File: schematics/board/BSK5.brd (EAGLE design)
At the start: 94 x 94 mm, 18 parts

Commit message: Новые схемы
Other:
- board text added: "BSK5 "Концерн ИТС""
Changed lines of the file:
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@@
 <text x="65.6" y="30.1" size="1.4224" layer="26" rot="MR0">BUS-</text>
 <text x="33.2" y="30.2" size="1.4224" layer="26" rot="MR0">BUS-</text>
+<text x="19.9" y="65.1" size="1.4224" layer="25" rot="MR45">BUS+</text>
+<text x="78.3" y="69.2" size="1.4224" layer="26" rot="MR315">BUS+</text>
+<text x="66.3" y="20.6" size="1.4224" layer="26" rot="MR225">BUS+</text>
+<text x="23.7" y="16.5" size="1.4224" layer="26" rot="MR135">BUS+</text>
+<text x="28.7" y="56.5" size="1.4224" layer="26" rot="MR45">BUS-</text>
+<text x="68.2" y="59.3" size="1.4224" layer="26" rot="MR315">BUS-</text>
+<text x="58.3" y="28.7" size="1.4224" layer="26" rot="MR225">BUS-</text>
+<text x="32.2" y="25" size="1.4224" layer="26" rot="MR135">BUS-</text>
+<text x="58.8" y="2.9" size="1.778" layer="25" rot="R180">BSK5 "Концерн ИТС"</text>
 </plain>
 <attributes>

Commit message: изменен БСК4
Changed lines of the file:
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@@
 <text x="65.6" y="30.1" size="1.4224" layer="26" rot="MR0">BUS-</text>
 <text x="33.2" y="30.2" size="1.4224" layer="26" rot="MR0">BUS-</text>
-<text x="19.9" y="65.1" size="1.4224" layer="25" rot="MR45">BUS+</text>
+<text x="19.9" y="65.1" size="1.4224" layer="26" rot="MR45">BUS+</text>
 <text x="78.3" y="69.2" size="1.4224" layer="26" rot="MR315">BUS+</text>
 <text x="66.3" y="20.6" size="1.4224" layer="26" rot="MR225">BUS+</text>
@@
 <text x="58.3" y="28.7" size="1.4224" layer="26" rot="MR225">BUS-</text>
 <text x="32.2" y="25" size="1.4224" layer="26" rot="MR135">BUS-</text>
-<text x="58.8" y="2.9" size="1.778" layer="25" rot="R180">BSK5 "Концерн ИТС"</text>
+<text x="35" y="3.8" size="1.778" layer="25" rot="MR180">BSK5 "Концерн ИТС"</text>
 </plain>
 <attributes>

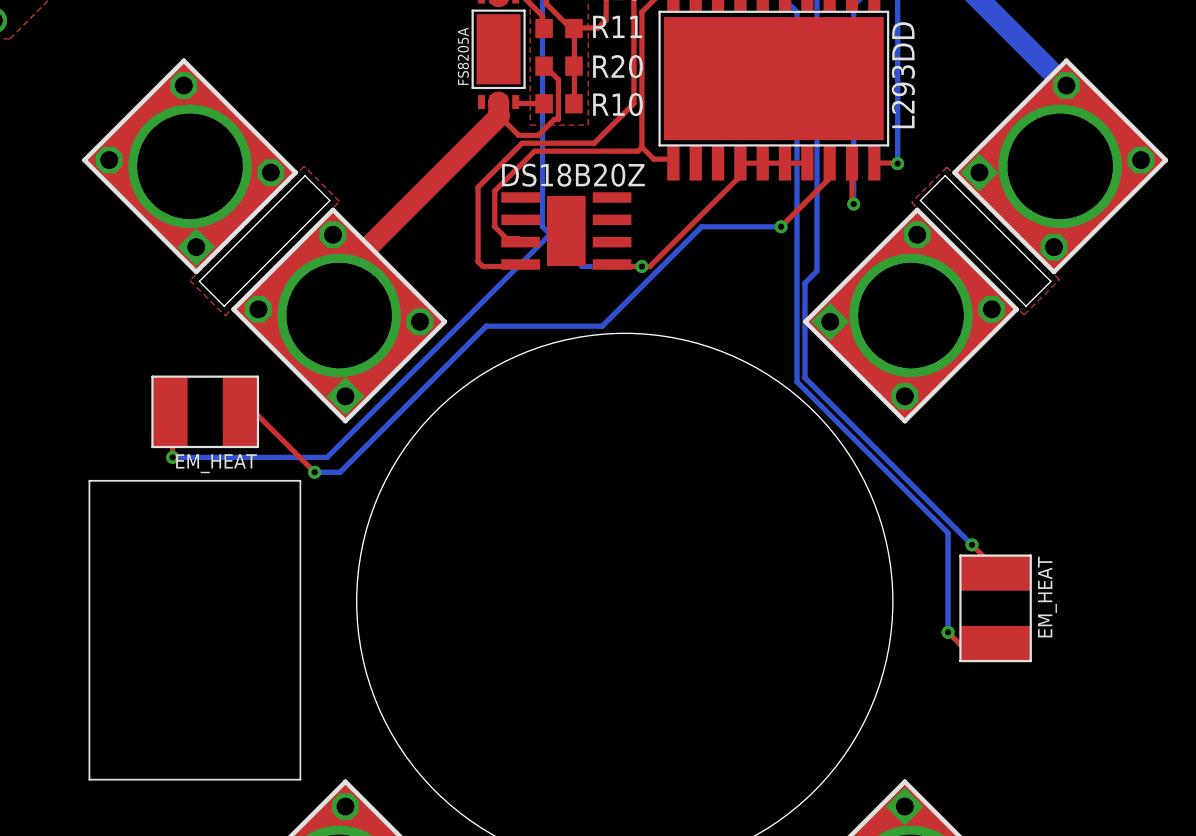
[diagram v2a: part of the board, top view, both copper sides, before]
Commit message: Добавлены светодиоды на платы БСК
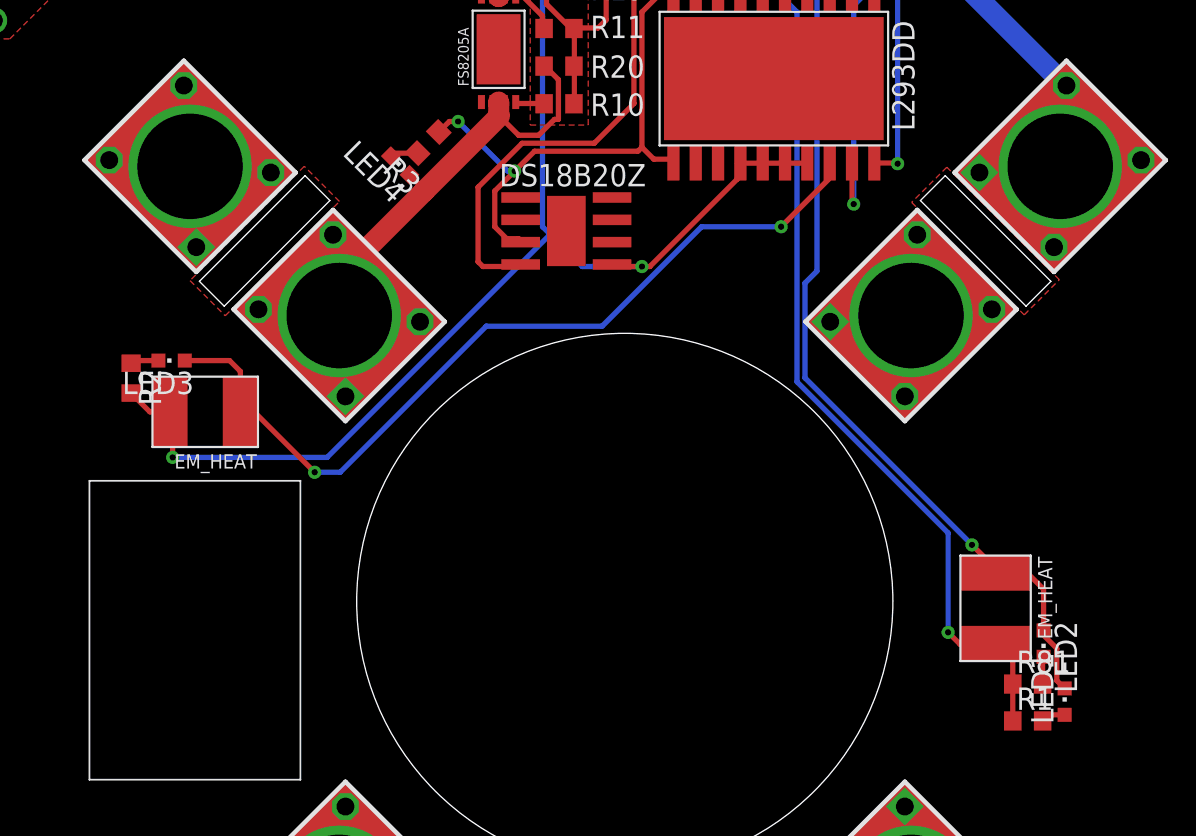
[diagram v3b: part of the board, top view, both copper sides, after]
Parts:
- added LED1, LED2, LED3, LED4: (no value), led:CHIPLED_0603
- added R1, R2, R3, R81: 2k, resistor:R0603
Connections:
- new net N$26: LED2.C, R81.2
- new net N$27: LED1.A, R1.2
- new net N$28: LED3.C, R2.1
- new net N$29: LED4.C, R3.2
- net 5V: now also R3.1
- net BUS-: now also LED4.A
- net GND: now also R2.2
- net N$1: now also LED1.C, LED2.A
- net N$2: now also R1.1, R81.1
- net N$3: now also LED3.A
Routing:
- net N$1: track 41.5 -> 50.8 mm
- net 5V: track 57.6 -> 63.3 mm, vias 2 -> 4
- net N$3: track 42.8 -> 48.5 mm
- net N$2: track 50.5 -> 55.4 mm
- net GND: track 93.1 -> 95.7 mm
- net N$28: track 0.00 -> 1.61 mm
- net N$29: track 0.00 -> 1.60 mm
- net N$26: track 0.00 -> 1.57 mm
- net N$27: track 0.00 -> 1.39 mm
- net BUS-: track 43.6 -> 44.8 mm

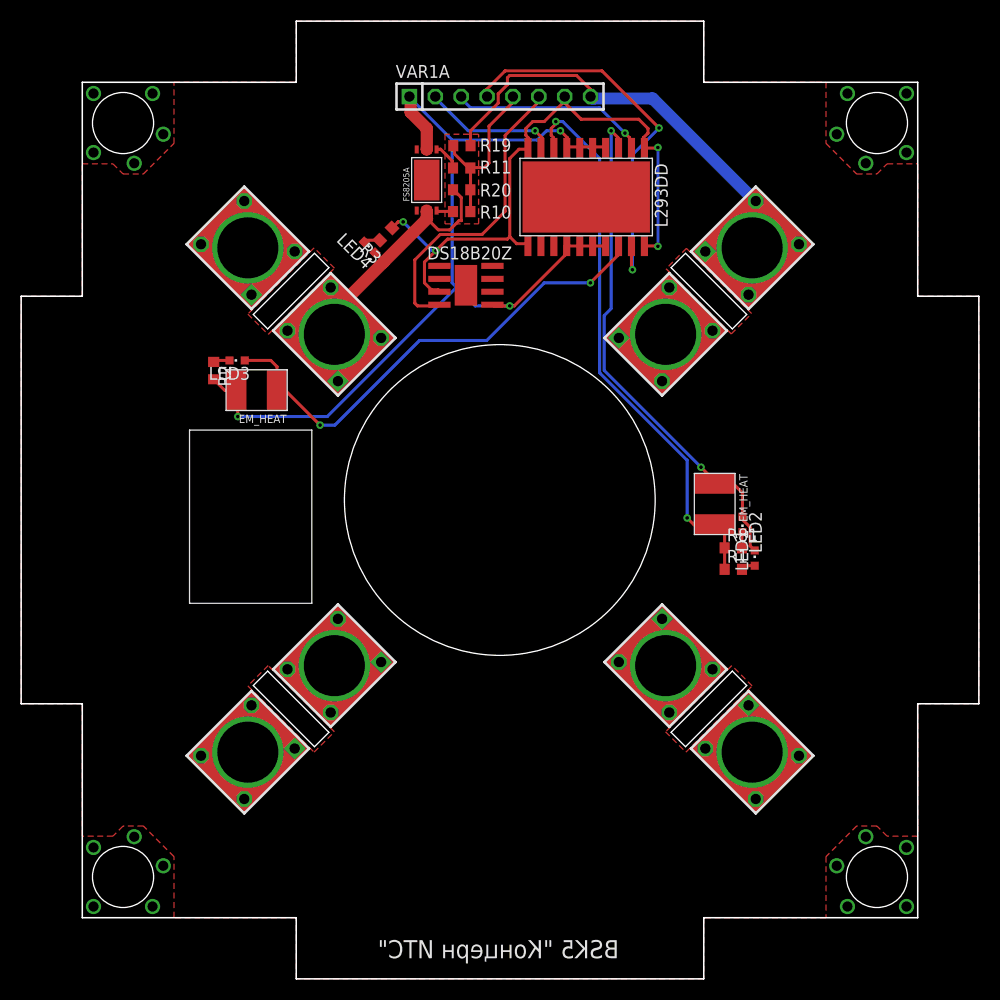
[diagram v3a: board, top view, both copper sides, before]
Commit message: Разведены платы БСК2-5
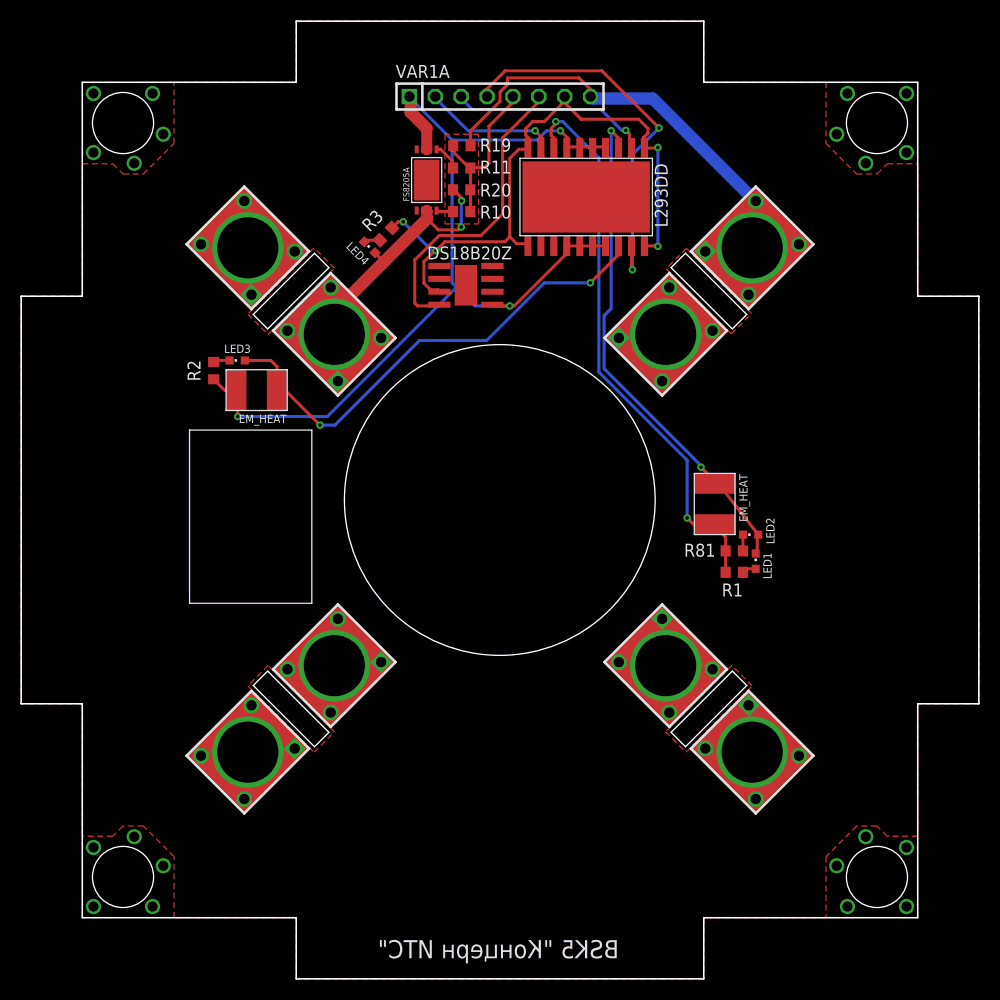
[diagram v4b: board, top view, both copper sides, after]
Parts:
- moved LED2 1.28 mm to (71.6, 43.6), turned to 90 degrees
- moved R1 0.32 mm to (70.0, 39.9)
- moved LED1 0.32 mm to (72.1, 41.0)
- moved R81 0.32 mm to (70.0, 42.0)
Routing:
- net N$1: track 50.8 -> 50.2 mm
- net BUS-: track 44.8 -> 45.3 mm, vias 0 -> 2
